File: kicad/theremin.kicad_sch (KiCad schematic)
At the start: 43 parts, among them J1 Eurorack Mono Jack, J3 Expression Attachment, SW1 SW_SPDT, U1 4069, U2 4069, U3 LM386, U4 LP2950-5.0_TO92

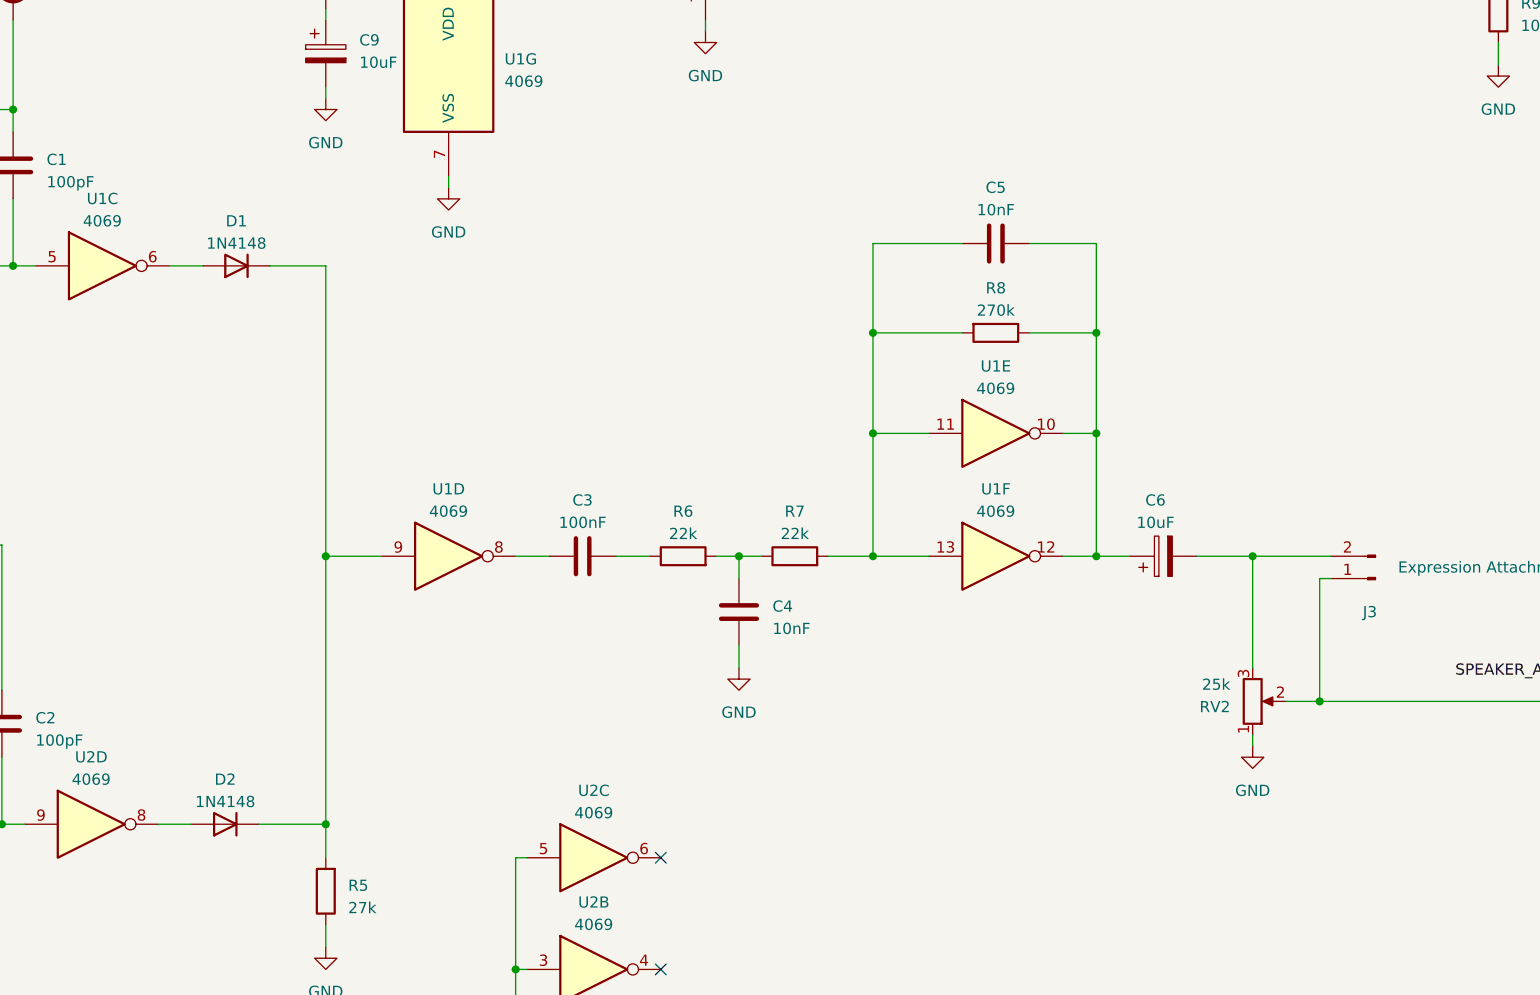
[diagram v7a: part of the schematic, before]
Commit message: Adding testpoints at output of oscillators
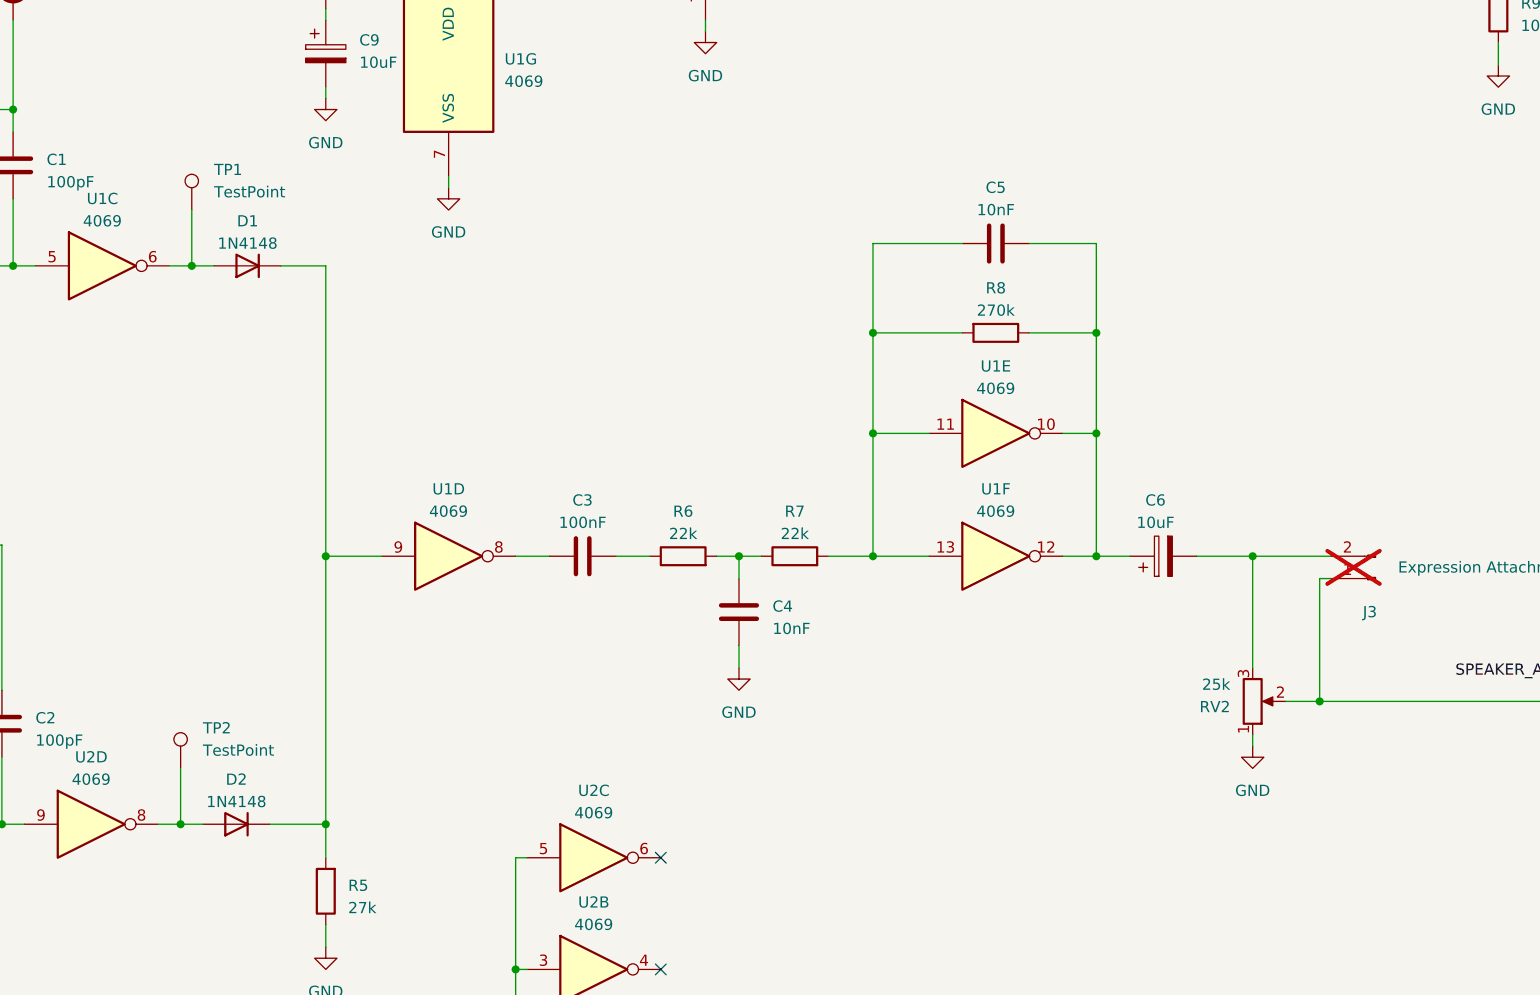
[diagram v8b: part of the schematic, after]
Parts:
- added TP1, TP2: TestPoint, Rumblesan_Standard_Parts:TestPoint_Loop_D2.50mm_Drill1.0mm_LowProfile, symbol Connector:TestPoint
- J3: now not fitted
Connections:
- net at D2.2 (A), U2.8: now also TP2.1
- net at D1.2 (A), U1.6: now also TP1.1
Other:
- moved on the sheet: D1, D2
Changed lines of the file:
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@@
 	)
 	(junction
+		(at 88.9 156.21)
+		(diameter 0)
+		(color 0 0 0 0)
+	)
+	(junction
 		(at 49.53 92.71)
 		(diameter 0)
@@
 	)
 	(junction
+		(at 90.17 92.71)
+		(diameter 0)
+		(color 0 0 0 0)
+	)
+	(junction
 		(at 68.58 156.21)
 		(diameter 0)
@@
 	(wire
 		(pts
-			(xy 87.63 92.71) (xy 91.44 92.71)
+			(xy 87.63 92.71) (xy 90.17 92.71)
 		)
 		(stroke
@@
 	(wire
 		(pts
+			(xy 88.9 156.21) (xy 91.44 156.21)
+		)
+		(stroke
+			(width 0)
+			(type default)
+		)
+	)
+	(wire
+		(pts
 			(xy 254 53.34) (xy 254 55.88)
 		)
@@
 	(wire
 		(pts
+			(xy 90.17 92.71) (xy 92.71 92.71)
+		)
+		(stroke
+			(width 0)
+			(type default)
+		)
+	)
+	(wire
+		(pts
 			(xy 68.58 148.59) (xy 68.58 156.21)
 		)
@@
 	(wire
 		(pts
-			(xy 99.06 92.71) (xy 105.41 92.71)
+			(xy 100.33 92.71) (xy 105.41 92.71)
 		)
 		(stroke
@@
 	(wire
 		(pts
+			(xy 88.9 149.86) (xy 88.9 156.21)
+		)
+		(stroke
+			(width 0)
+			(type default)
+		)
+	)
+	(wire
+		(pts
 			(xy 260.35 24.13) (xy 260.35 25.4)
 		)
@@
 	(wire
 		(pts
+			(xy 90.17 86.36) (xy 90.17 92.71)
+		)
+		(stroke
+			(width 0)
+			(type default)
+		)
+	)
+	(wire
+		(pts
 			(xy 105.41 156.21) (xy 105.41 160.02)
 		)
@@
 	(wire
 		(pts
-			(xy 97.79 156.21) (xy 105.41 156.21)
+			(xy 99.06 156.21) (xy 105.41 156.21)
 		)
 		(stroke
@@
 	(wire
 		(pts
-			(xy 86.36 156.21) (xy 90.17 156.21)
+			(xy 86.36 156.21) (xy 88.9 156.21)
 		)
 		(stroke
@@
 	(symbol
 		(lib_id "Diode:1N4148")
-		(at 93.98 156.21 180)
+		(at 95.25 156.21 180)
 		(unit 1)
 		(exclude_from_sim no)
@@
 		(fields_autoplaced yes)
 		(property "Reference" "D2"
-			(at 93.98 151.13 0)
+			(at 95.25 151.13 0)
 			(effects
 				(font
@@
 		)
 		(property "Value" "1N4148"
-			(at 93.98 153.67 0)
+			(at 95.25 153.67 0)
 			(effects
 				(font
@@
 		)
 		(property "Footprint" "Diode_THT:D_DO-35_SOD27_P7.62mm_Horizontal"
-			(at 93.98 156.21 0)
+			(at 95.25 156.21 0)
 			(effects
 				(font
@@
 		)
 		(property "Datasheet" "https://assets.nexperia.com/documents/data-sheet/1N4148_1N4448.pdf"
-			(at 93.98 156.21 0)
+			(at 95.25 156.21 0)
 			(effects
 				(font
@@
 		)
 		(property "Description" ""
-			(at 93.98 156.21 0)
+			(at 95.25 156.21 0)
 			(effects
 				(font
@@
 		)
 		(property "Sim.Device" "D"
-			(at 93.98 156.21 0)
+			(at 95.25 156.21 0)
 			(effects
 				(font
@@
 		)
 		(property "Sim.Pins" "1=K 2=A"
-			(at 93.98 156.21 0)
+			(at 95.25 156.21 0)
 			(effects
 				(font
@@
 	(symbol
 		(lib_id "Diode:1N4148")
-		(at 95.25 92.71 180)
+		(at 96.52 92.71 180)
 		(unit 1)
 		(exclude_from_sim no)
@@
 		(fields_autoplaced yes)
 		(property "Reference" "D1"
-			(at 95.25 87.63 0)
+			(at 96.52 87.63 0)
 			(effects
 				(font
@@
 		)
 		(property "Value" "1N4148"
-			(at 95.25 90.17 0)
+			(at 96.52 90.17 0)
 			(effects
 				(font
@@
 		)
 		(property "Footprint" "Diode_THT:D_DO-35_SOD27_P7.62mm_Horizontal"
-			(at 95.25 92.71 0)
+			(at 96.52 92.71 0)
 			(effects
 				(font
@@
 		)
 		(property "Datasheet" "https://assets.nexperia.com/documents/data-sheet/1N4148_1N4448.pdf"
-			(at 95.25 92.71 0)
+			(at 96.52 92.71 0)
 			(effects
 				(font
@@
 		)
 		(property "Description" ""
-			(at 95.25 92.71 0)
+			(at 96.52 92.71 0)
 			(effects
 				(font
@@
 		)
 		(property "Sim.Device" "D"
-			(at 95.25 92.71 0)
+			(at 96.52 92.71 0)
 			(effects
 				(font
@@
 		)
 		(property "Sim.Pins" "1=K 2=A"
-			(at 95.25 92.71 0)
+			(at 96.52 92.71 0)
 			(effects
 				(font
@@
 	)
 	(symbol
+		(lib_id "Connector:TestPoint")
+		(at 88.9 149.86 0)
+		(unit 1)
+		(exclude_from_sim no)
+		(in_bom yes)
+		(on_board yes)
+		(dnp no)
+		(fields_autoplaced yes)
+		(property "Reference" "TP2"
+			(at 91.44 145.2879 0)
+			(effects
+				(font
+					(size 1.27 1.27)
+				)
+				(justify left)
+			)
+		)
+		(property "Value" "TestPoint"
+			(at 91.44 147.8279 0)
+			(effects
+				(font
+					(size 1.27 1.27)
+				)
+				(justify left)
+			)
+		)
+		(property "Footprint" "Rumblesan_Standard_Parts:TestPoint_Loop_D2.50mm_Drill1.0mm_LowProfile"
+			(at 93.98 149.86 0)
+			(effects
+				(font
+					(size 1.27 1.27)
+				)
+				(hide yes)
+			)
+		)
+		(property "Datasheet" "~"
+			(at 93.98 149.86 0)
+			(effects
+				(font
+					(size 1.27 1.27)
+				)
+				(hide yes)
+			)
+		)
+		(property "Description" "test point"
+			(at 88.9 149.86 0)
+			(effects
+				(font
+					(size 1.27 1.27)
+				)
+				(hide yes)
+			)
+		)
+		(pin "1"
+		)
+		(instances
+			(project "theremin"
+				(path "/5b0acaca-dc50-4fa5-b146-164c1b9ad031"
+					(reference "TP2")
+					(unit 1)
+				)
+			)
+		)
+	)
+	(symbol
 		(lib_id "Device:R")
 		(at 57.15 29.21 90)
@@
 	)
 	(symbol
+		(lib_id "Connector:TestPoint")
+		(at 90.17 86.36 0)
+		(unit 1)
+		(exclude_from_sim no)
+		(in_bom yes)
+		(on_board yes)
+		(dnp no)
+		(fields_autoplaced yes)
+		(property "Reference" "TP1"
+			(at 92.71 81.7879 0)
+			(effects
+				(font
+					(size 1.27 1.27)
+				)
+				(justify left)
+			)
+		)
+		(property "Value" "TestPoint"
+			(at 92.71 84.3279 0)
+			(effects
+				(font
+					(size 1.27 1.27)
+				)
+				(justify left)
+			)
+		)
+		(property "Footprint" "Rumblesan_Standard_Parts:TestPoint_Loop_D2.50mm_Drill1.0mm_LowProfile"
+			(at 95.25 86.36 0)
+			(effects
+				(font
+					(size 1.27 1.27)
+				)
+				(hide yes)
+			)
+		)
+		(property "Datasheet" "~"
+			(at 95.25 86.36 0)
+			(effects
+				(font
+					(size 1.27 1.27)
+				)
+				(hide yes)
+			)
+		)
+		(property "Description" "test point"
+			(at 90.17 86.36 0)
+			(effects
+				(font
+					(size 1.27 1.27)
+				)
+				(hide yes)
+			)
+		)
+		(pin "1"
+		)
+		(instances
+			(project ""
+				(path "/5b0acaca-dc50-4fa5-b146-164c1b9ad031"
+					(reference "TP1")
+					(unit 1)
+				)
+			)
+		)
+	)
+	(symbol
 		(lib_id "Device:C")
 		(at 68.58 144.78 180)
@@
 		(in_bom no)
 		(on_board yes)
-		(dnp no)
+		(dnp yes)
 		(property "Reference" "J3"
 			(at 224.155 132.08 0)
